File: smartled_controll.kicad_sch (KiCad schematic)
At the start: 49 parts, among them J1 Conn_01x04, U1 OC5028B, U2 MAX485E, U3 STM8S003F3P, U4 OC5864

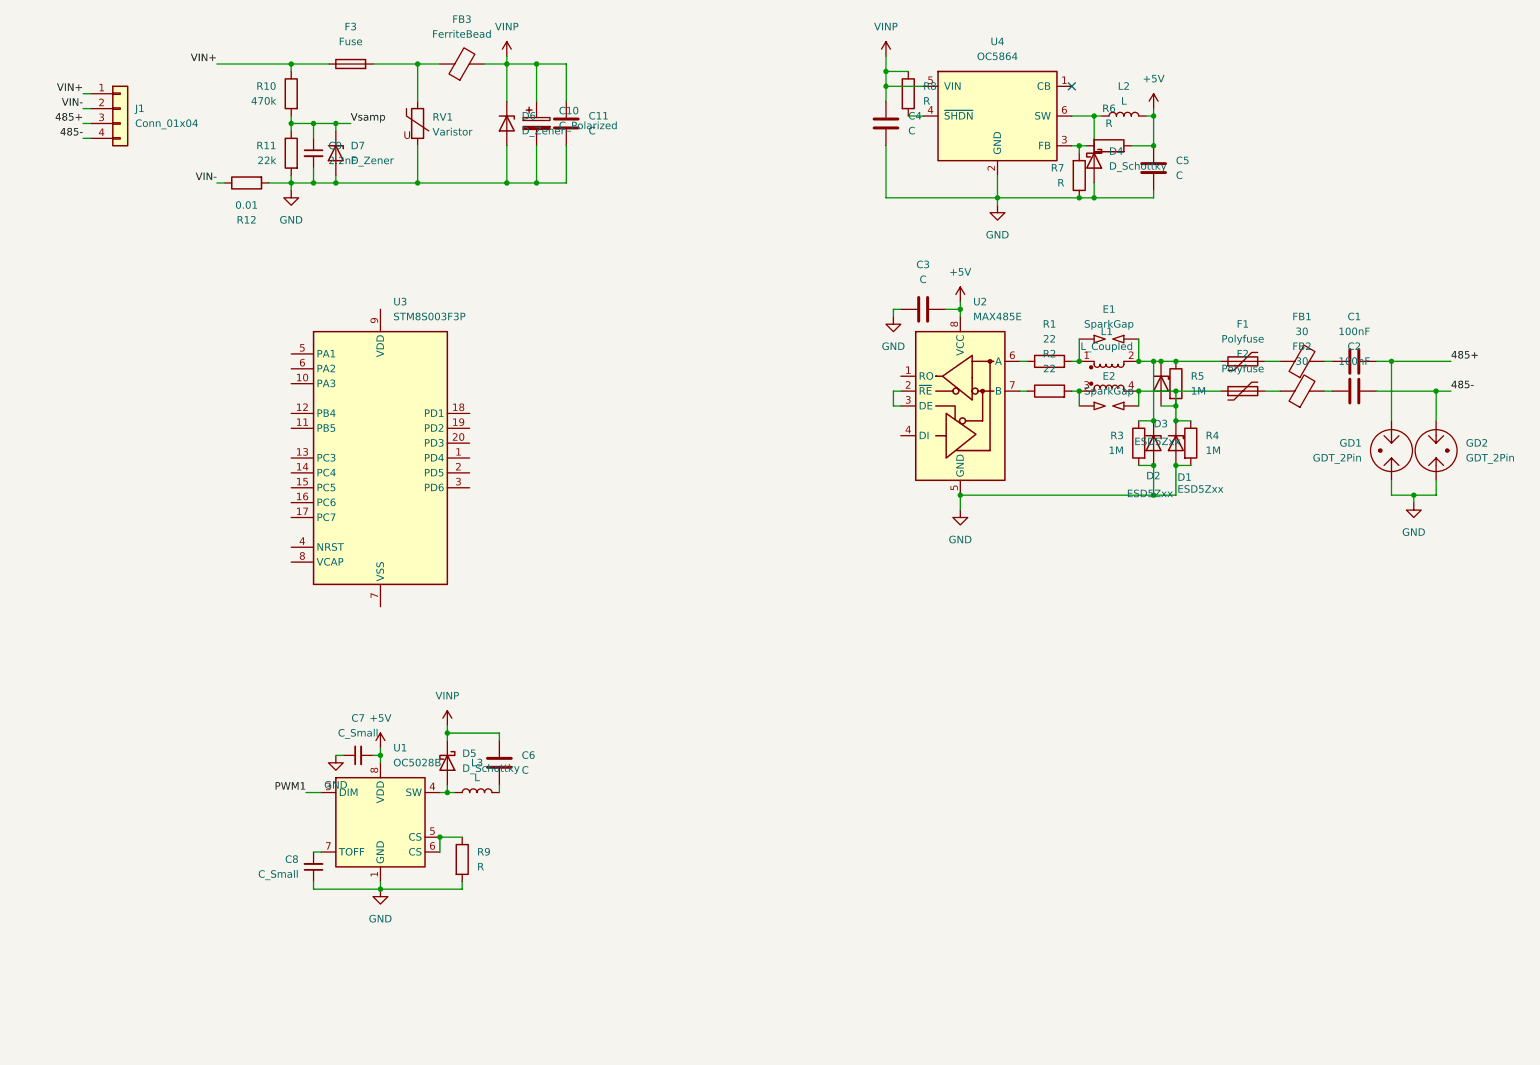
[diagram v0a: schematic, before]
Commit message: 单片机换为PY32F003F1xUx（自己制作符号），添加3.3V LDO电路，电流采样放大电路，按键，温度和光照传感器
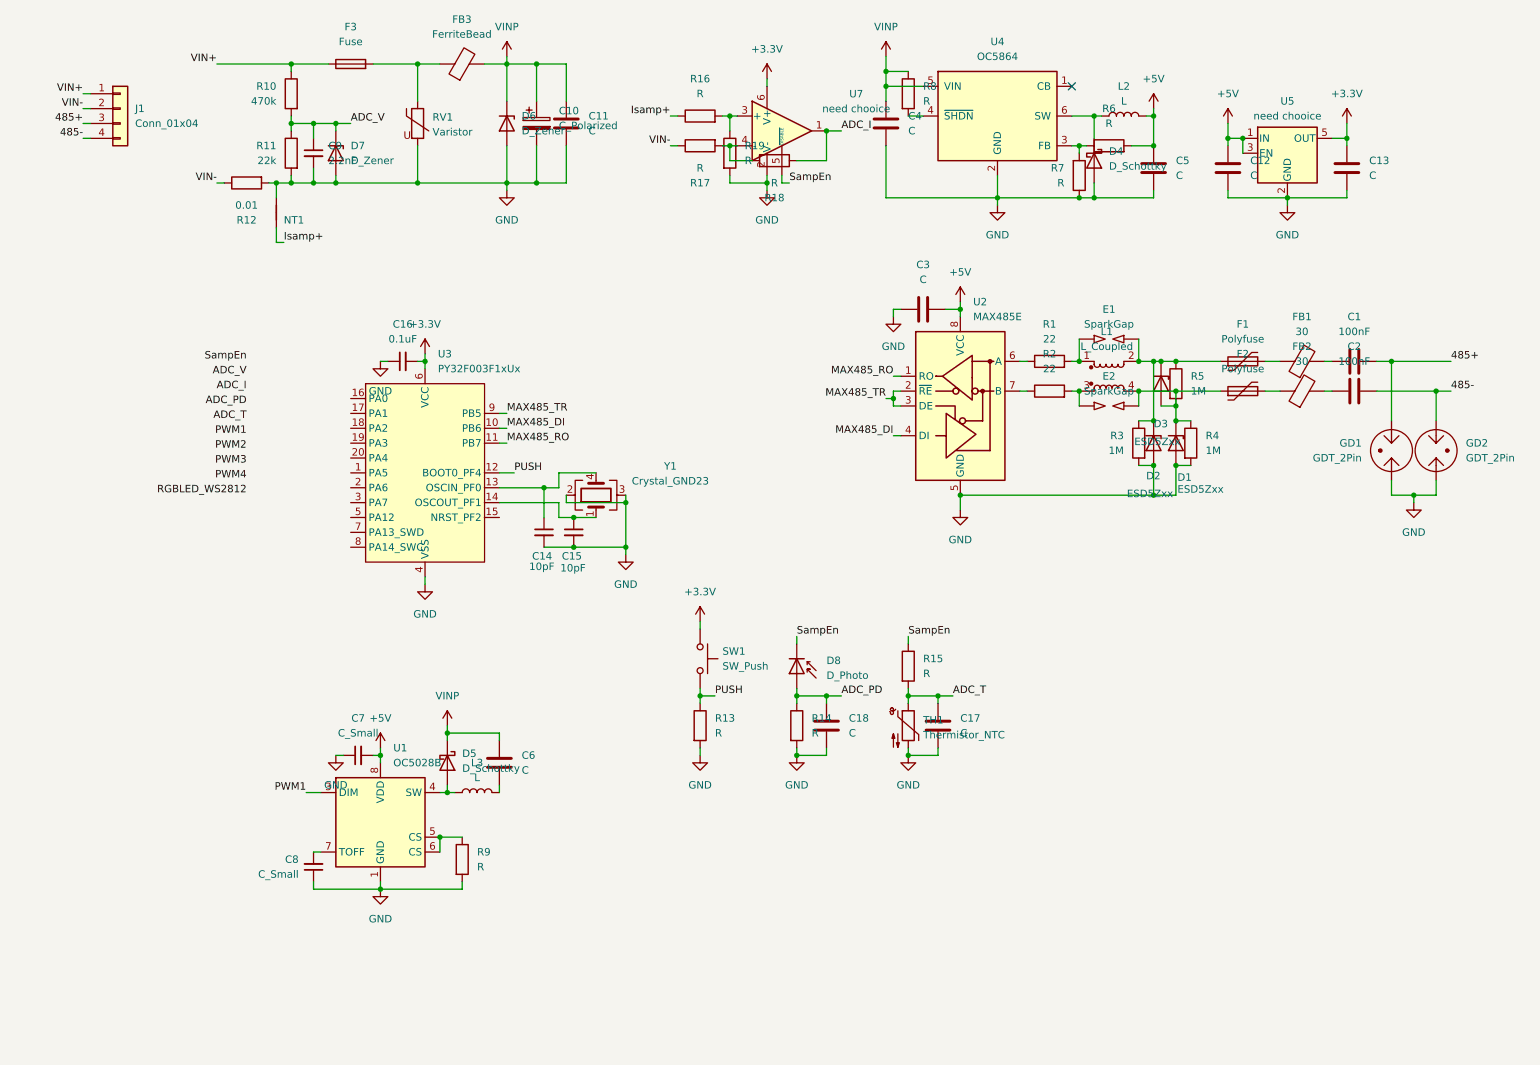
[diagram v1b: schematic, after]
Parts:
- removed U3: STM8S003F3P, Package_SO:TSSOP-20_4.4x6.5mm_P0.65mm, symbol MCU_ST_STM8:STM8S003F3P
- added C12, C13, C17, C18: C, symbol Device:C
- added C14, C15: 10pF, symbol Device:C_Small
- added C16: 0.1uF, symbol Device:C_Small
- added D8: D_Photo, symbol Device:D_Photo
- added NT1: NetTie_2, symbol Device:NetTie_2
- added R13, R14, R15, R16, R17, R18, R19: R, symbol Device:R
- added SW1: SW_Push, symbol Switch:SW_Push
- added TH1: Thermistor_NTC, symbol Device:Thermistor_NTC
- added U3: PY32F003F1xUx, Package_DFN_QFN:QFN-20-1EP_3x3mm_P0.4mm_EP1.65x1.65mm, symbol project_syms:PY32F003F1xUx
- added U5: need chooice, Package_TO_SOT_SMD:SOT-23-5, symbol Regulator_Linear:TLV70033_SOT23-5
- added U7: need chooice, Package_TO_SOT_SMD:SOT-23-6, symbol Amplifier_Operational:ADA4807-1
- added Y1: Crystal_GND23, symbol Device:Crystal_GND23
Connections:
- net +5V: now also C12.1, U5.1 (IN), U5.3 (EN)
- net GND: now also C12.2, C13.2, C14.2, C15.2, C16.1, C17.2, C18.2, NT1.1, R13.2, R14.2, R19.2, TH1.2, U3.4 (VSS), U5.2 (GND), U7.2 (V-), Y1.2, Y1.3
- net VIN-: now also R17.1
- net MAX485_RO: now reaches U2.1 (RO)
- net MAX485_RO: now also U3.11 (PB7)
- net MAX485_TR: now reaches U2.2 (~{RE}), U2.3 (DE)
- net MAX485_TR: now also U3.9 (PB5)
- net MAX485_DI: now reaches U2.4 (DI)
- net MAX485_DI: now also U3.10 (PB6)
- net Vsamp renamed ADC_V
- new net: R17.2, R18.2, U7.4 (-)
- new net: R16.2, R19.1, U7.3 (+)
- new net: C15.1, U3.14 (OSCOUT_PF1), Y1.1
- new net: C14.1, U3.13 (OSCIN_PF0), Y1.4
- new net +3.3V: C13.1, C16.2, SW1.1, U3.6 (VCC), U5.5 (OUT), U7.6 (V+)
- new net ADC_I: R18.1, U7.1
- new net ADC_PD: C18.1, D8.2 (A), R14.1
- new net ADC_T: C17.1, R15.2, TH1.1
- new net Isamp+: NT1.2, R16.1
- new net PUSH: R13.1, SW1.2, U3.12 (BOOT0_PF4)
- new net SampEn: D8.1 (K), R15.1, U7.5 (~{DISABLE})

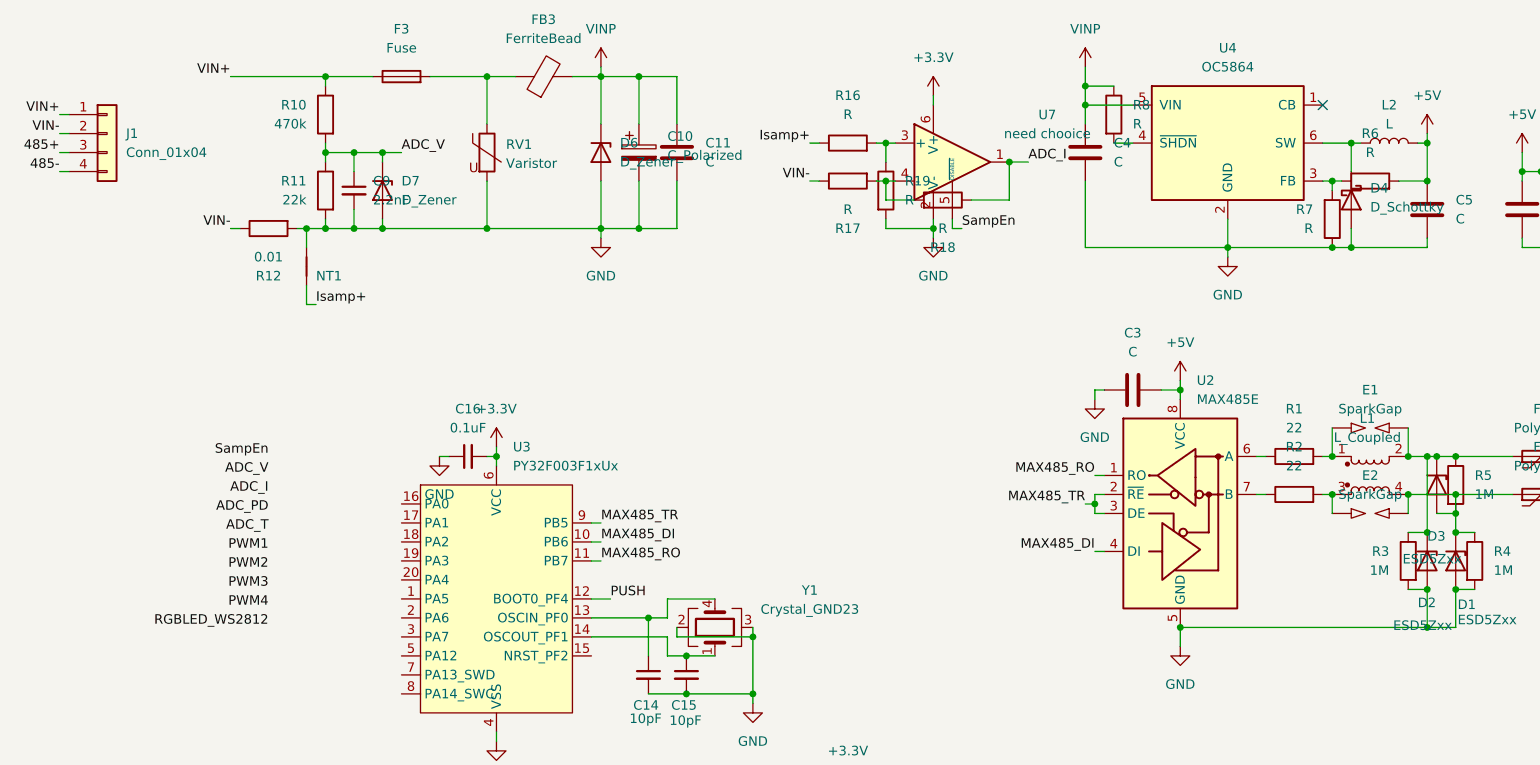
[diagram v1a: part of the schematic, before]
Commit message: 在PCB上放置各电路模块的元器件大致布局，少量修改原理图
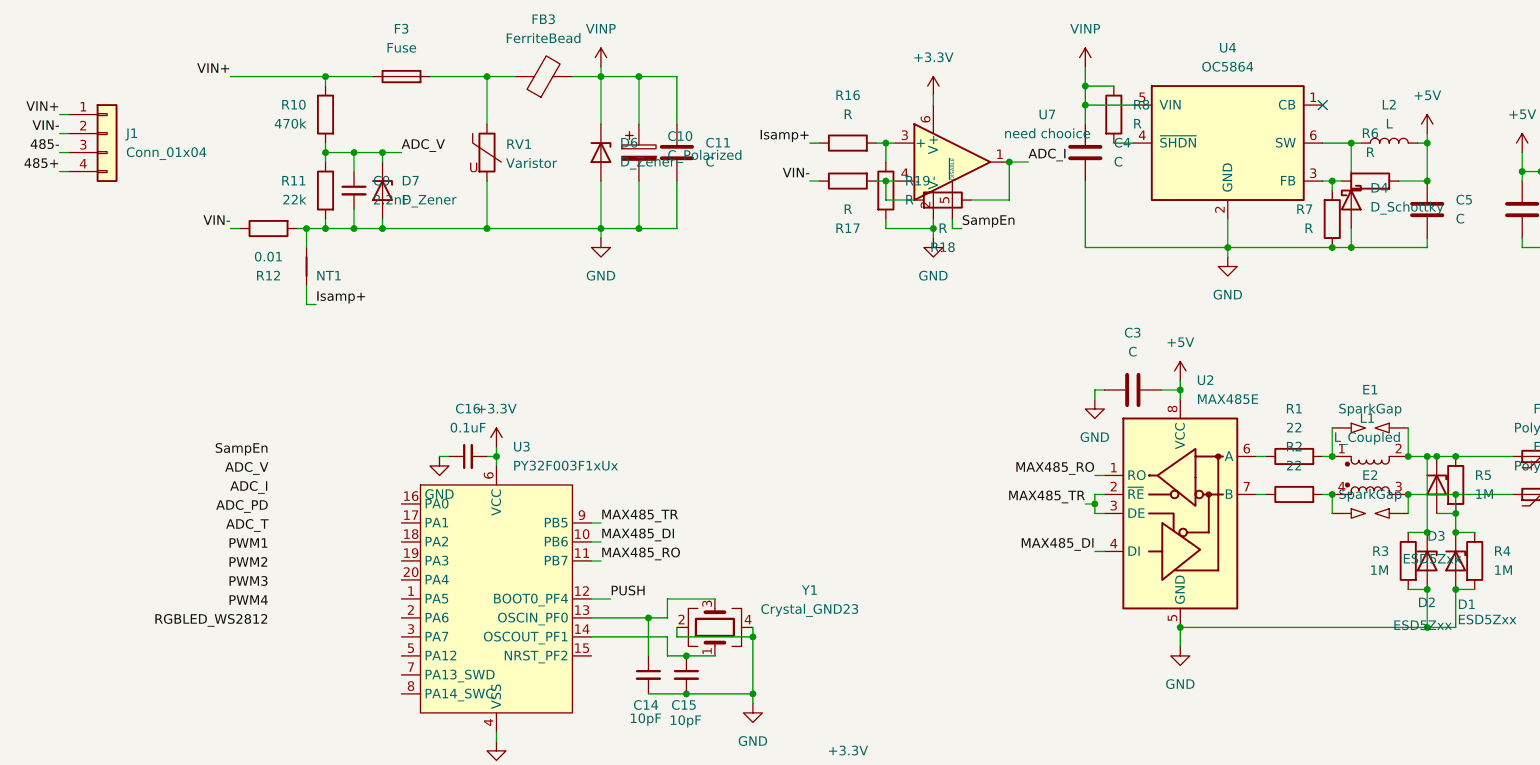
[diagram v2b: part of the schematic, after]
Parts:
- C12, C13: footprint (none) -> Capacitor_SMD:C_0805_2012Metric
- C14, C15, C16, C17, C18: footprint (none) -> Capacitor_SMD:C_0402_1005Metric
- D7: footprint Diode_SMD:D_SMA -> Diode_SMD:D_SOD-123F
- D8, TH1: footprint (none) -> Connector_PinHeader_1.00mm:PinHeader_1x02_P1.00mm_Vertical
- L1: symbol Device:L_Coupled -> Device:L_Coupled_1243
- NT1: footprint (none) -> NetTie:NetTie-2_SMD_Pad0.5mm
- R13, R14, R15, R16, R17, R18, R19: footprint (none) -> Resistor_SMD:R_0402_1005Metric
- R8: footprint Resistor_SMD:R_0603_1608Metric -> Resistor_SMD:R_0402_1005Metric
- SW1: footprint (none) -> Button_Switch_SMD:SW_Push_SPST_NO_Alps_SKRK
- Y1: footprint (none) -> Crystal:Crystal_SMD_2016-4Pin_2.0x1.6mm; symbol Device:Crystal_GND23 -> Device:Crystal_GND24
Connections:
- net 485+: now also J1.4 (Pin_4); no longer J1.3 (Pin_3)
- net 485-: now also J1.3 (Pin_3); no longer J1.4 (Pin_4)
- net GND: now also Y1.4; no longer Y1.3
- net at E2.1, R2.2: now also L1.4; no longer L1.3
- net at C14.1, U3.13 (OSCIN_PF0): now also Y1.3; no longer Y1.4
- net at D1.1 (K), D3.2 (A), E2.2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: now also L1.3; no longer L1.4
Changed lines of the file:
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@@
 		)
 	)
-	(label "VIN+"
-		(at 45.72 29.21 180)
+	(label "485-"
+		(at 22.86 39.37 180)
 		(effects
 			(font
@@
 	)
 	(label "485+"
-		(at 22.86 39.37 180)
+		(at 22.86 41.91 180)
+		(effects
+			(font
+				(size 1.27 1.27)
+			)
+			(justify right bottom)
+		)
+	)
+	(label "VIN+"
+		(at 45.72 29.21 180)
 		(effects
 			(font
@@
 		)
 	)
-	(label "485-"
-		(at 22.86 41.91 180)
-		(effects
-			(font
-				(size 1.27 1.27)
-			)
-			(justify right bottom)
-		)
-	)
 	(label "VIN+"
 		(at 22.86 34.29 180)
@@
 			)
 		)
-		(property "Footprint" ""
+		(property "Footprint" "Capacitor_SMD:C_0402_1005Metric"
 			(at 169.8752 146.05 0)
 			(effects
@@
 			)
 		)
-		(property "Footprint" ""
+		(property "Footprint" "Connector_PinHeader_1.00mm:PinHeader_1x02_P1.00mm_Vertical"
 			(at 144.78 132.08 0)
 			(effects
@@
 			)
 		)
-		(property "Footprint" ""
+		(property "Footprint" "Capacitor_SMD:C_0805_2012Metric"
 			(at 219.4052 50.8 0)
 			(effects
@@
 			)
 		)
-		(property "Footprint" ""
+		(property "Footprint" "Capacitor_SMD:C_0402_1005Metric"
 			(at 77.47 80.01 0)
 			(effects
@@
 			)
 		)
-		(property "Footprint" ""
+		(property "Footprint" "Connector_PinHeader_1.00mm:PinHeader_1x02_P1.00mm_Vertical"
 			(at 163.83 140.97 0)
 			(effects
@@
 			)
 		)
-		(property "Footprint" ""
+		(property "Footprint" "Resistor_SMD:R_0402_1005Metric"
 			(at 128.27 41.402 90)
 			(effects
@@
 			)
 		)
-		(property "Footprint" ""
+		(property "Footprint" "Resistor_SMD:R_0402_1005Metric"
 			(at 140.97 47.498 90)
 			(effects
@@
 			)
 		)
-		(property "Footprint" "Diode_SMD:D_SMA"
+		(property "Footprint" "Diode_SMD:D_SOD-123F"
 			(at 66.04 44.45 0)
 			(effects
@@
 			)
 		)
-		(property "Footprint" ""
+		(property "Footprint" "Resistor_SMD:R_0402_1005Metric"
 			(at 131.572 44.45 90)
 			(effects
@@
 	)
 	(symbol
-		(lib_id "Device:Crystal_GND23")
+		(lib_id "Device:Crystal_GND24")
 		(at 110.49 102.87 90)
 		(unit 1)
@@
 			)
 		)
-		(property "Footprint" ""
+		(property "Footprint" "Crystal:Crystal_SMD_2016-4Pin_2.0x1.6mm"
 			(at 110.49 102.87 0)
 			(effects
@@
 			)
 		)
-		(property "Description" "Four pin crystal, GND on pins 2 and 3"
+		(property "Description" "Four pin crystal, GND on pins 2 and 4"
 			(at 110.49 102.87 0)
 			(effects
@@
 			)
 		)
-		(property "Footprint" ""
+		(property "Footprint" "Button_Switch_SMD:SW_Push_SPST_NO_Alps_SKRK"
 			(at 133.35 130.81 0)
 			(effects
@@
 			)
 		)
-		(property "Footprint" ""
+		(property "Footprint" "Resistor_SMD:R_0402_1005Metric"
 			(at 143.002 142.24 90)
 			(effects
@@
 			)
 		)
-		(property "Footprint" ""
+		(property "Footprint" "Capacitor_SMD:C_0402_1005Metric"
 			(at 150.8252 146.05 0)
 			(effects
@@
 			)
 		)
-		(property "Footprint" ""
+		(property "Footprint" "NetTie:NetTie-2_SMD_Pad0.5mm"
 			(at 55.88 54.61 0)
 			(effects
@@
 			)
 		)
-		(property "Footprint" ""
+		(property "Footprint" "Resistor_SMD:R_0402_1005Metric"
 			(at 162.052 132.08 90)
 			(effects
@@
 			)
 		)
-		(property "Footprint" ""
+		(property "Footprint" "Resistor_SMD:R_0402_1005Metric"
 			(at 126.492 142.24 90)
 			(effects
@@
 			)
 		)
-		(property "Footprint" ""
+		(property "Footprint" "Capacitor_SMD:C_0402_1005Metric"
 			(at 101.6 109.22 0)
 			(effects
@@
 	)
 	(symbol
-		(lib_id "Device:L_Coupled")
+		(lib_id "Device:L_Coupled_1243")
 		(at 198.12 82.55 0)
 		(unit 1)
@@
 		(on_board yes)
 		(dnp no)
-		(fields_autoplaced yes)
 		(property "Reference" "L1"
 			(at 197.739 74.93 0)
@@
 			)
 		)
-		(property "Footprint" ""
+		(property "Footprint" "Capacitor_SMD:C_0402_1005Metric"
 			(at 106.68 109.22 0)
 			(effects
@@
 			)
 		)
-		(property "Footprint" ""
+		(property "Footprint" "Capacitor_SMD:C_0805_2012Metric"
 			(at 239.7252 50.8 0)
 			(effects
@@
 			)
 		)
-		(property "Footprint" ""
+		(property "Footprint" "Resistor_SMD:R_0402_1005Metric"
 			(at 128.27 39.878 90)
 			(effects
@@
 			)
 		)
-		(property "Footprint" "Resistor_SMD:R_0603_1608Metric"
+		(property "Footprint" "Resistor_SMD:R_0402_1005Metric"
 			(at 162.052 34.29 90)
 			(effects
